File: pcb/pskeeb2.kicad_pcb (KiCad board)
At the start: 2 copper layers, 98 x 91.5 mm, 29 parts, among them K11 KEYSW, K12 KEYSW, K13 KEYSW, K14 KEYSW, K15 KEYSW, K21 KEYSW, K22 KEYSW, K23 KEYSW, K24 KEYSW, K25 KEYSW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

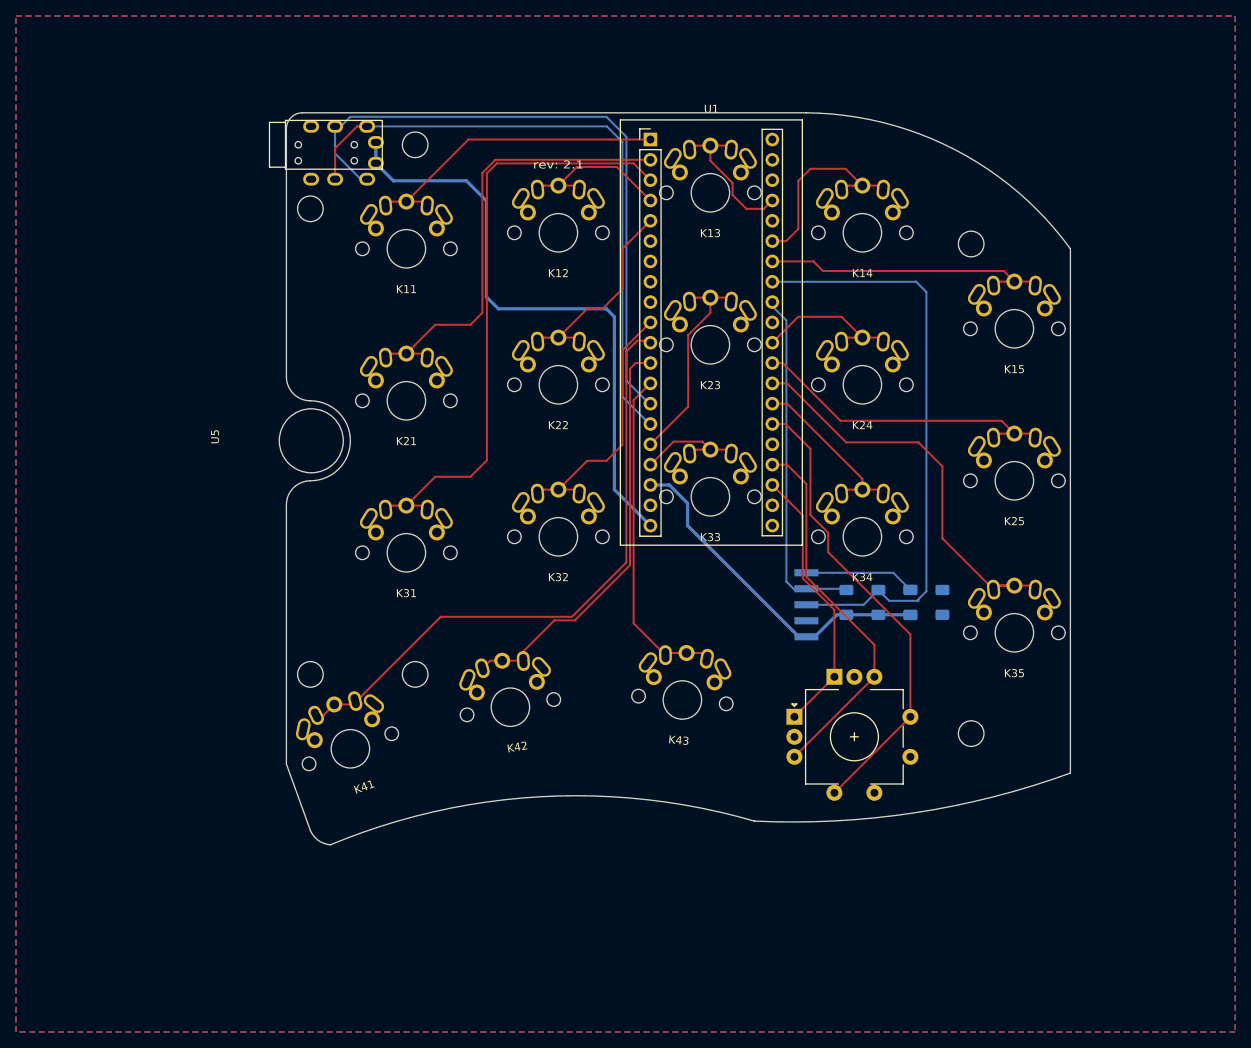
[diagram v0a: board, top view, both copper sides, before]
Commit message: fix: leave more space for soldering / use gh1.25 socket for trackpoint
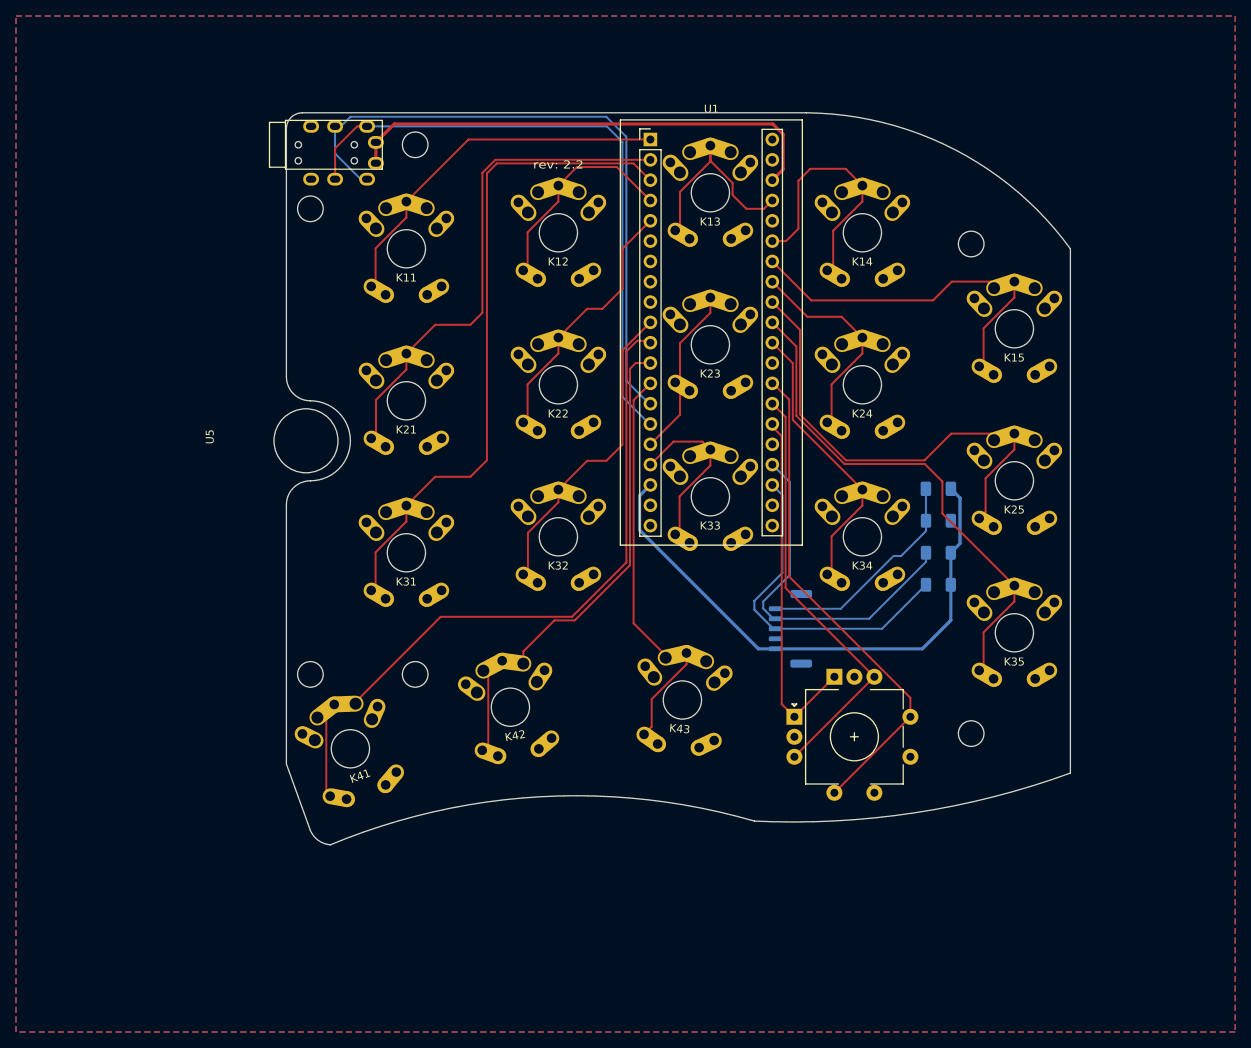
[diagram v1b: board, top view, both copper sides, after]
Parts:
- K11, K12, K13, K14, K15, K21, K22, K23, K24, K25, K31, K32, K33, K34, K35, K41, K42, K43: footprint kwkb-footprint:Mx-Choc-Reversible -> kwkb-footprint:Mx-Choc-Rev
- U4: footprint kwkb-footprint:HY20_1x05_P2.00mm_Vertical_SMD -> Connector_JST:JST_GH_SM05B-GHS-TB_1x05-1MP_P1.25mm_Horizontal
- moved C1 14.6 mm to (163.0, 80.0), turned to 180 degrees
- moved R2 13.1 mm to (163.0, 88.0), turned to 180 degrees
- moved R3 10.2 mm to (163.0, 84.0), turned to 0 degrees
- moved R1 7.82 mm to (163.0, 92.0), turned to 180 degrees
- moved U4 3.35 mm to (144.5, 97.5), turned to -90 degrees
- moved U5 0.66 mm to (76.0, 74.0)
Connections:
- U1 pad 20: +3V3 -> unconnected-(U1-Pad20)
- U1 pad 23: ENA -> TP_CLK
- U1 pad 24: ENB -> TP_DAT
- U1 pad 26: /k44 -> ENA
- U1 pad 27: /k34 -> ENB
- U1 pad 28: /k35 -> /k44
- U1 pad 29: /k25 -> unconnected-(U1-Pad29)
- U1 pad 30: /k24 -> /k34
- U1 pad 31: unconnected-(U1-Pad31) -> /k35
- U1 pad 32: TP_DAT -> /k25
- U1 pad 33: TP_CLK -> /k24
- U1 pad 38: unconnected-(U1-Pad38) -> +3V3
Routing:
- net TP_CLK: track 74.1 -> 42.3 mm
- net +5V: track 43.1 -> 70.1 mm
- net /k25: track 39.5 -> 59.2 mm
- net TP_RST: track 13.9 -> 28.1 mm
- net +3V3: track 75.4 -> 61.3 mm
- net /k34: track 22.1 -> 35.9 mm
- net /k35: track 51.3 -> 63.7 mm
- net ENA: track 34.3 -> 44.8 mm
- net /k15: track 37.9 -> 47.3 mm
- net /k24: track 19.6 -> 26.6 mm
- net /k32: track 32.7 -> 39.5 mm
- net /k33: track 14.7 -> 21.6 mm
- net /k31: track 75.7 -> 82.5 mm
- net /k21: track 56.4 -> 63.2 mm
- net /k14: track 25.0 -> 31.8 mm
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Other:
- board text added: "rev: 2.2"
- board text removed: "100k/2.2uF/4.7k/4.7k"
- board text removed: "rev: 2.1"

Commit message: chore: rev 2.4
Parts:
- SW1, SW2: footprint Keebio-Parts:RotaryEncoder_EC11-no-legs -> kwkb-footprint:RotaryEncoder_EC11-no-legs
- moved SW1 11.5 mm to (163.5, 114.5)
- moved SW2 4.74 mm to (151.0, 106.5), turned to 0 degrees
- moved U4 2.50 mm to (143.0, 95.5)
- moved U1 1.34 mm to (126.9, 35.0)
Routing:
- net ENA: track 44.8 -> 67.9 mm
- net TX: track 81.5 -> 78.2 mm
- net ENB: track 53.6 -> 55.9 mm
- net /k44: track 62.4 -> 64.5 mm
- net /k35: track 63.7 -> 65.1 mm
- net /k25: track 59.2 -> 60.6 mm
- net /k34: track 35.9 -> 37.3 mm
- net /k22: track 32.9 -> 34.2 mm
- net /k43: track 48.9 -> 50.2 mm
- net TP_RST: track 28.1 -> 29.3 mm
- net /k14: track 31.8 -> 30.8 mm
- net /k23: track 21.4 -> 20.4 mm
- net TP_DAT: track 45.3 -> 46.2 mm
- net /k15: track 47.3 -> 48.0 mm
- net /k24: track 26.6 -> 27.2 mm
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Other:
- board size 98 x 91.5 mm -> 98 x 92 mm
- board text added: "rev: 2.4"
- board text removed: "R/D/C/G/V"
- board text removed: "rev: 2.2"

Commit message: feat: releasing 2.5
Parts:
- moved SW1 2.50 mm to (163.5, 117.0)
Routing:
- net ENA: track 67.9 -> 56.4 mm
- net ENB: track 55.9 -> 57.6 mm
- net /k44: track 64.5 -> 65.6 mm
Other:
- board text added: "rev: 2.5"
- board text removed: "rev: 2.4"
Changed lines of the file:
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@@
   )
   (footprint "kwkb-footprint:RotaryEncoder_EC11-no-legs" (layer "F.Cu")
-    (at 163.5 114.5)
+    (at 163.5 117)
     (descr "Alps rotary encoder, EC12E... with switch, vertical shaft, http://www.alps.com/prod/info/E/HTML/Encoder/Incremental/EC11/EC11E15204A3.html")
     (tags "rotary encoder")
@@
   (gr_arc (start 81.5 34.9) (mid 82.120711 33.550767) (end 83.5 33) (layer "Edge.Cuts") (width 0.1))
   (gr_arc (start 84.5 69) (mid 89.5 74) (end 84.5 79) (layer "Edge.Cuts") (width 0.1))
-  (gr_text "rev: 2.4" (at 115.5 39.5) (layer "F.SilkS")
+  (gr_text "rev: 2.5" (at 115.5 39.5) (layer "F.SilkS")
     (effects (font (size 1 1.2) (thickness 0.15)))
   )
@@
   (segment (start 144.6 86.4) (end 139.7 91.3) (width 0.25) (layer "B.Cu") (net 24))
   (segment (start 141 107.5) (end 142.5 109) (width 0.25) (layer "F.Cu") (net 25))
-  (segment (start 158 118) (end 158 114) (width 0.25) (layer "F.Cu") (net 25))
+  (segment (start 150.5 109) (end 156 114.5) (width 0.25) (layer "F.Cu") (net 25))
   (segment (start 143.45 102.05) (end 141 104.5) (width 0.25) (layer "F.Cu") (net 25))
   (segment (start 142.14 70.56) (end 143.45 71.87) (width 0.25) (layer "F.Cu") (net 25))
+  (segment (start 143.5 109) (end 150.5 109) (width 0.25) (layer "F.Cu") (net 25))
   (segment (start 142.5 109) (end 143.5 109) (width 0.25) (layer "F.Cu") (net 25))
   (segment (start 141 104.5) (end 141 107.5) (width 0.25) (layer "F.Cu") (net 25))
-  (segment (start 154 119.5) (end 156.5 119.5) (width 0.25) (layer "F.Cu") (net 25))
   (segment (start 143.45 71.87) (end 143.45 102.05) (width 0.25) (layer "F.Cu") (net 25))
-  (segment (start 158 114) (end 156 112) (width 0.25) (layer "F.Cu") (net 25))
-  (segment (start 156.5 119.5) (end 158 118) (width 0.25) (layer "F.Cu") (net 25))
-  (segment (start 143.5 109) (end 154 119.5) (width 0.25) (layer "F.Cu") (net 25))
   (segment (start 143.9 103.6) (end 143.5 104) (width 0.25) (layer "F.Cu") (net 26))
   (segment (start 142.14 68.02) (end 143.9 69.78) (width 0.25) (layer "F.Cu") (net 26))
-  (segment (start 143.5 104) (end 151.5 112) (width 0.25) (layer "F.Cu") (net 26))
-  (segment (start 151.5 112) (end 151.5 114) (width 0.25) (layer "F.Cu") (net 26))
-  (segment (start 151.5 114) (end 154.5 117) (width 0.25) (layer "F.Cu") (net 26))
   (segment (start 143.9 69.78) (end 143.9 103.6) (width 0.25) (layer "F.Cu") (net 26))
-  (segment (start 154.5 117) (end 156 117) (width 0.25) (layer "F.Cu") (net 26))
+  (segment (start 151 111.5) (end 151 114.5) (width 0.25) (layer "B.Cu") (net 26))
+  (segment (start 151 114.5) (end 156 119.5) (width 0.25) (layer "B.Cu") (net 26))
+  (segment (start 143.5 104) (end 151 111.5) (width 0.25) (layer "B.Cu") (net 26))
   (segment (start 155 106) (end 158 109) (width 0.25) (layer "F.Cu") (net 27))
-  (segment (start 161 112) (end 170.5 112) (width 0.25) (layer "F.Cu") (net 27))
-  (segment (start 158 109) (end 161 112) (width 0.25) (layer "F.Cu") (net 27))
   (segment (start 144.35 95.35) (end 155.5 106.5) (width 0.25) (layer "F.Cu") (net 27))
   (segment (start 144.35 67.69) (end 144.35 95.35) (width 0.25) (layer "F.Cu") (net 27))
   (segment (start 142.14 65.48) (end 144.35 67.69) (width 0.25) (layer "F.Cu") (net 27))
+  (segment (start 158 109) (end 163.5 114.5) (width 0.25) (layer "F.Cu") (net 27))
+  (segment (start 163.5 114.5) (end 170.5 114.5) (width 0.25) (layer "F.Cu") (net 27))
   (segment (start 87.5875 34.7) (end 87.5875 38.0875) (width 0.25) (layer "B.Cu") (net 34))
   (segment (start 128.075 71.046701) (end 128.075 69.175) (width 0.25) (layer "B.Cu") (net 34))
